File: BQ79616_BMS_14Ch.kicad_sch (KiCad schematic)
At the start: 163 parts, among them J1 Conn_02x10_Odd_Even, J2 Conn_02x10_Odd_Even, J3 Conn_Therm, J4 BMS_A_IN, J5 BMS_A_OUT, Q1 MMBT5551

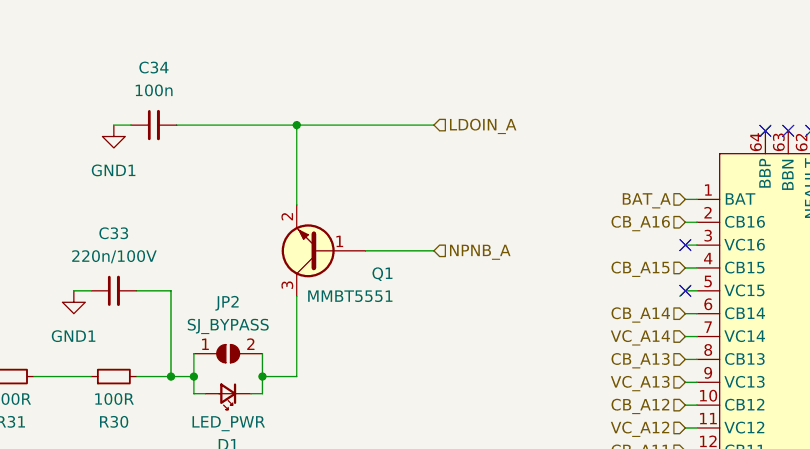
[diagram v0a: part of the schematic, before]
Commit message: Fill all 3D model including connector and transformer
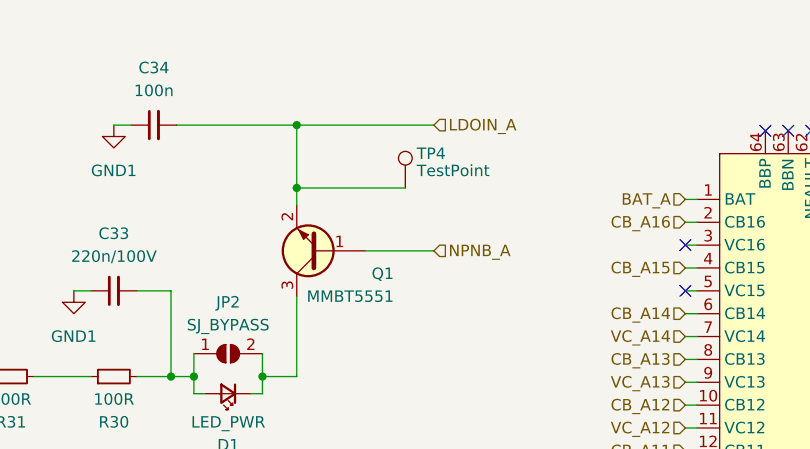
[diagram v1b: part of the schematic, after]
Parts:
- added TP4: TestPoint, symbol Connector:TestPoint
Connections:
- net LDOIN_A: now also TP4.1
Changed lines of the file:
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@@
   (junction (at 170.18 266.7) (diameter 0) (color 0 0 0 0)
   )
+  (junction (at 76.835 34.29) (diameter 0) (color 0 0 0 0)
+  )
   (junction (at 90.17 231.14) (diameter 0) (color 0 0 0 0)
   )
@@
     (stroke (width 0) (type default))
   )
+  (wire (pts (xy 76.835 34.29) (xy 88.9 34.29))
+    (stroke (width 0) (type default))
+  )
   (wire (pts (xy 71.755 182.88) (xy 71.755 185.42))
     (stroke (width 0) (type default))
@@
     (stroke (width 0) (type default))
   )
-  (wire (pts (xy 76.835 27.305) (xy 76.835 36.195))
+  (wire (pts (xy 76.835 27.305) (xy 76.835 34.29))
     (stroke (width 0) (type default))
   )
@@
     (stroke (width 0) (type default) (color 0 0 255 0.98))
   )
+  (wire (pts (xy 76.835 34.29) (xy 76.835 36.195))
+    (stroke (width 0) (type default))
+  )
   (wire (pts (xy 71.755 228.6) (xy 71.755 240.03))
     (stroke (width 0) (type default))
@@
         )
       )
+    )
+  )
+  (symbol (lib_id "Connector:TestPoint") (at 88.9 34.29 0) (unit 1)
+    (in_bom yes) (on_board yes) (dnp no)
+    (property "Reference" "TP4" (at 90.17 30.48 0)
+      (effects (font (size 1.27 1.27)) (justify left))
+    )
+    (property "Value" "TestPoint" (at 90.17 32.385 0)
+      (effects (font (size 1.27 1.27)) (justify left))
+    )
+    (property "Footprint" "" (at 93.98 34.29 0)
+      (effects (font (size 1.27 1.27)) hide)
+    )
+    (property "Datasheet" "~" (at 93.98 34.29 0)
+      (effects (font (size 1.27 1.27)) hide)
+    )
+    (pin "1")
+    (instances
+      (project "BQ79616_BMS_14Ch"
+        (path "/0ff84c0c-cd95-4e37-82ee-50268bd68af4"
+          (reference "TP4") (unit 1)
+        )
+      )
